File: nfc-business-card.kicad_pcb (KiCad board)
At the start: 2 copper layers, 89 x 51 mm, 4 parts, among them U1 NT3H2111W0FHKH

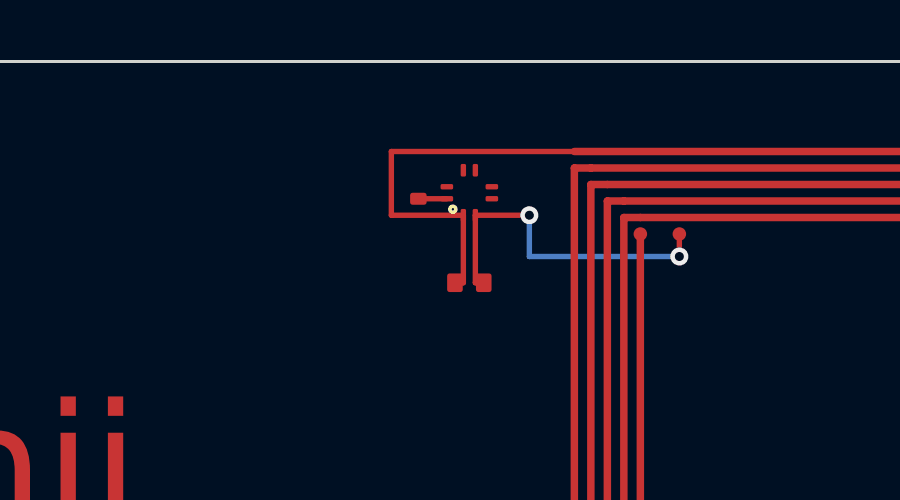
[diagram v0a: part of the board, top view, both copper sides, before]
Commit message: feat(stability): NC pull-downs, C1 BOM fix, and tuned assembly exports
Add DNP R2–R6 (100 kΩ to VSS on B.Cu) for floating NC pins, lock C1 to
Walsin 10 pF NP0 (C301961), and export bom-c1/positions-c1 for JLC SMT.
Correct wrong LCSC IDs in parts.md and add tune_antenna.py for C1/turn trim.

Co-authored-by: Cursor <cursoragent@cursor.com>
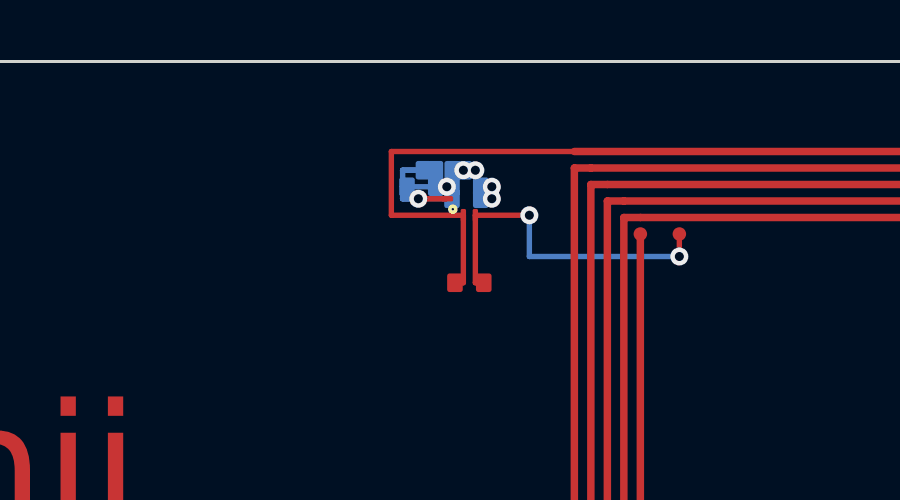
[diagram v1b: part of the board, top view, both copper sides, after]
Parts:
- added R2: DNP, NFC_BusinessCard:R_0402_1005Metric, B.Cu at (51.9, 4.17)
- added R3: DNP, NFC_BusinessCard:R_0402_1005Metric, B.Cu at (52.9, 3.62)
- added R4: DNP, NFC_BusinessCard:R_0402_1005Metric, B.Cu at (52.4, 3.62)
- added R5: DNP, NFC_BusinessCard:R_0402_1005Metric, B.Cu at (53.4, 4.17)
- added R6: DNP, NFC_BusinessCard:R_0402_1005Metric, B.Cu at (53.4, 4.58)
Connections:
- U1 pad 3: (no net) -> SCL
- U1 pad 4: (no net) -> FD
- U1 pad 5: (no net) -> SDA
- U1 pad 6: (no net) -> VCC
- U1 pad 7: (no net) -> VOUT
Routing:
- net GND: track 0.95 -> 7.65 mm, vias 0 -> 1
- net SDA: track 0.00 -> 0.37 mm, vias 0 -> 1
- net VOUT: track 0.00 -> 0.37 mm, vias 0 -> 1
- net VCC: track 0.00 -> 0.37 mm, vias 0 -> 1
- net SCL: track 0.00 -> 0.37 mm, vias 0 -> 1
- net FD: track 0.00 -> 0.37 mm, vias 0 -> 1
